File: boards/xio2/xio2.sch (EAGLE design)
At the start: 337 parts, among them J1 12401598E4#2A, Q1 BSS138, Q2 BSS138, Q3 BC817-16LT3G, Q4 BC817-16LT3G, X1 MINI-USB-UX60-MB-5ST, Y2 FA-238 25.0000MB-K3

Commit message: Latest schematic and routed board
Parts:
- renumbered CART_SLOT to HOST_IO, U$1 to XIO, X1 to USB
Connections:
- net N$1 renamed XIO_CLK_OUT
- net N$2 renamed XIO_CLK_IN

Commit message: Update some BOM-related things
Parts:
- C105, C93, C95: device rcl:C-EUC0402 -> rcl:C-EUC0402K
- C177: device rcl:C-EUC0201 -> rcl:C-EUC0402
- CARTRIDGE: value A8_CART -> 5650118-1

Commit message: Some small notes on layout
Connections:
- net N$72 renamed XSPI5_MISO_R
- net N$73 renamed XSPI5_MOSI_R
- net N$74 renamed XSPI5_SCK_R
- net N$75 renamed XSPI6_MISO_R
- net N$79 renamed XSPI6_SCK_R
- net N$98 renamed XSPI6_MOSI_R
- net XPSI5_MOSI renamed XSPI5_MOSI
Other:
- moved on the sheet: R91, R92, R93

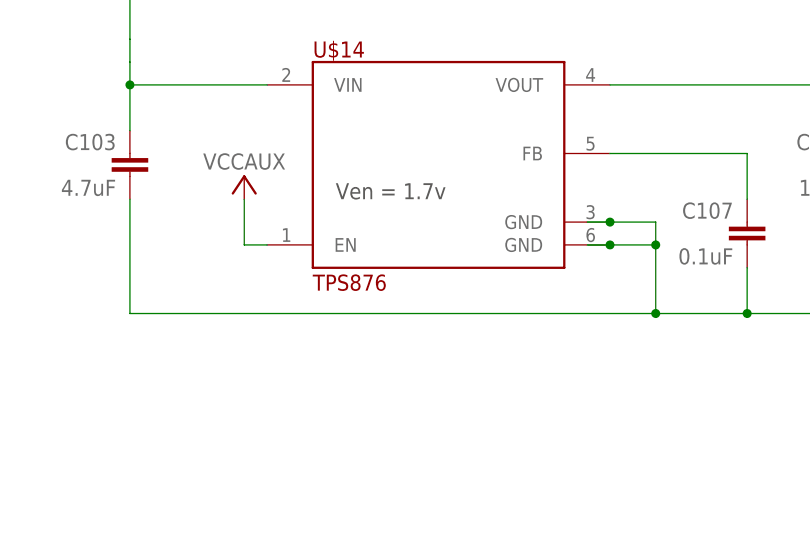
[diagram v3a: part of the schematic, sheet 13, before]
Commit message: Update the TI vreg
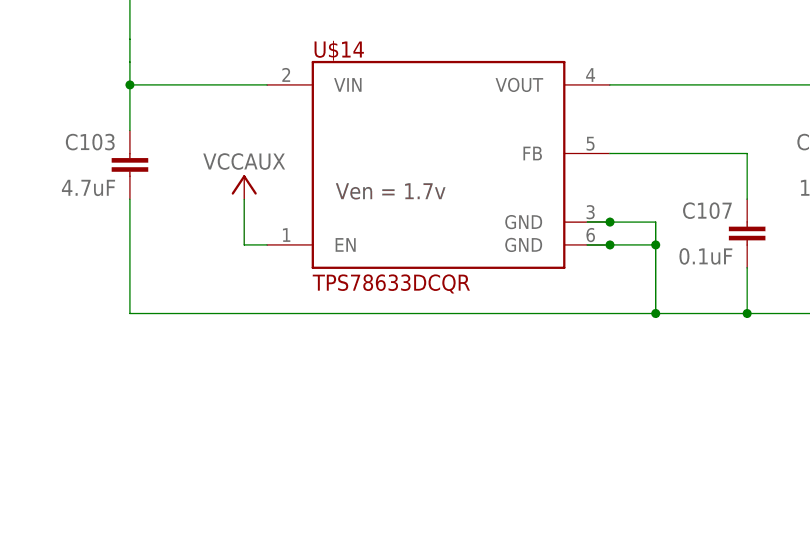
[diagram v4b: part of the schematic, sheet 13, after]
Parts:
- U$14: value TPS876 -> TPS78633DCQR
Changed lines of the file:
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@@
 <part name="LED3" library="led" library_urn="urn:adsk.eagle:library:259" deviceset="LED" device="CHIPLED_0603" package3d_urn="urn:adsk.eagle:package:15822/2" value="LTST-S270GKT"/>
 <part name="SUPPLY90" library="supply2" deviceset="GND" device=""/>
-<part name="U$14" library="sjg-power" deviceset="TPS876" device="" package3d_urn="urn:adsk.eagle:package:4768344/1"/>
+<part name="U$14" library="sjg-power" deviceset="TPS876" device="" package3d_urn="urn:adsk.eagle:package:4768344/1" value="TPS78633DCQR"/>
 <part name="C107" library="rcl" library_urn="urn:adsk.eagle:library:334" deviceset="C-EU" device="C0201" package3d_urn="urn:adsk.eagle:package:23690/2" value="0.1uF"/>
 <part name="C103" library="rcl" library_urn="urn:adsk.eagle:library:334" deviceset="C-EU" device="C0402" package3d_urn="urn:adsk.eagle:package:23626/1" value="4.7uF"/>

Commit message: Design review first changes
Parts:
- renumbered U$14 to FPGA_VCCO
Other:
- note added: "TMDS_33 signalling requires 50R pull-ups to 3.3v on all inputs. Labels {RX*,TX*} are from perspective of the host board, so need to add pull-ups to TX* lines on this board. Will dissipate 66mA, so need to be 0603"
- note removed: "TMDS_33 signalling requires 50R pull-ups to 3.3v on all inputs. Labels {RX*,TX*} are from perspective of the host board, so need to add pull-ups to TX* lines on this board."
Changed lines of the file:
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@@
 <part name="LED3" library="led" library_urn="urn:adsk.eagle:library:259" deviceset="LED" device="CHIPLED_0603" package3d_urn="urn:adsk.eagle:package:15822/2" value="LTST-S270GKT"/>
 <part name="SUPPLY90" library="supply2" deviceset="GND" device=""/>
-<part name="U$14" library="sjg-power" deviceset="TPS876" device="" package3d_urn="urn:adsk.eagle:package:4768344/1" value="TPS78633DCQR"/>
+<part name="FPGA_VCCO" library="sjg-power" deviceset="TPS876" device="" package3d_urn="urn:adsk.eagle:package:4768344/1" value="TPS78633DCQR"/>
 <part name="C107" library="rcl" library_urn="urn:adsk.eagle:library:334" deviceset="C-EU" device="C0201" package3d_urn="urn:adsk.eagle:package:23690/2" value="0.1uF"/>
 <part name="C103" library="rcl" library_urn="urn:adsk.eagle:library:334" deviceset="C-EU" device="C0402" package3d_urn="urn:adsk.eagle:package:23626/1" value="4.7uF"/>
@@
 <pinref part="+3V23" gate="G$1" pin="+3V3"/>
 <wire x1="96.52" y1="93.98" x2="96.52" y2="99.06" width="0.1524" layer="91"/>
+<label x="93.98" y="104.14" size="1.778" layer="95"/>
 </segment>
 </net>
@@
 <wire x1="-124.46" y1="76.2" x2="-124.46" y2="78.74" width="0.1524" layer="91"/>
 <junction x="-124.46" y="78.74"/>
+<label x="-127" y="96.52" size="1.778" layer="95"/>
 </segment>
 <segment>
@@
 <wire x1="-127" y1="-35.56" x2="-127" y2="-33.02" width="0.1524" layer="91"/>
 <junction x="-127" y="-33.02"/>
+<label x="-129.54" y="-20.32" size="1.778" layer="95"/>
 </segment>
 <segment>
@@
 <wire x1="-127" y1="22.86" x2="-127" y2="25.4" width="0.1524" layer="91"/>
 <junction x="-127" y="25.4"/>
+<label x="-129.54" y="40.64" size="1.778" layer="95"/>
 </segment>
 </net>
@@
 <instance part="U$7" gate="G$1" x="73.66" y="63.5"/>
 <instance part="U$8" gate="G$1" x="73.66" y="104.14"/>
-<instance part="U$14" gate="G$1" x="-124.46" y="-86.36"/>
+<instance part="FPGA_VCCO" gate="G$1" x="-124.46" y="-86.36"/>
 <instance part="C107" gate="G$1" x="-88.9" y="-93.98" rot="MR0"/>
 <instance part="C103" gate="G$1" x="-157.48" y="-86.36" rot="MR0"/>
@@
 <wire x1="-99.06" y1="-93.98" x2="-99.06" y2="-96.52" width="0.1524" layer="91"/>
 <junction x="-99.06" y="-96.52"/>
-<pinref part="U$14" gate="G$1" pin="GND@TAB"/>
+<pinref part="FPGA_VCCO" gate="G$1" pin="GND@TAB"/>
 <junction x="-104.14" y="-96.52"/>
-<pinref part="U$14" gate="G$1" pin="GND@3"/>
+<pinref part="FPGA_VCCO" gate="G$1" pin="GND@3"/>
 <junction x="-104.14" y="-93.98"/>
 <pinref part="C107" gate="G$1" pin="2"/>
@@
 <wire x1="-144.78" y1="-96.52" x2="-144.78" y2="-91.44" width="0.1524" layer="91"/>
 <pinref part="U$6" gate="G$1" pin="VCCAUX"/>
-<pinref part="U$14" gate="G$1" pin="EN@1"/>
+<pinref part="FPGA_VCCO" gate="G$1" pin="EN@1"/>
 </segment>
 <segment>
@@
 <wire x1="-157.48" y1="-83.82" x2="-157.48" y2="-78.74" width="0.1524" layer="91"/>
 <pinref part="C103" gate="G$1" pin="1"/>
-<pinref part="U$14" gate="G$1" pin="VIN@2"/>
+<pinref part="FPGA_VCCO" gate="G$1" pin="VIN@2"/>
 <wire x1="-157.48" y1="-78.74" x2="-157.48" y2="-76.2" width="0.1524" layer="91"/>
 <wire x1="-142.24" y1="-78.74" x2="-157.48" y2="-78.74" width="0.1524" layer="91"/>
@@
 <segment>
 <pinref part="C107" gate="G$1" pin="1"/>
-<pinref part="U$14" gate="G$1" pin="FB@5"/>
+<pinref part="FPGA_VCCO" gate="G$1" pin="FB@5"/>
 <wire x1="-88.9" y1="-91.44" x2="-88.9" y2="-86.36" width="0.1524" layer="91"/>
 <wire x1="-88.9" y1="-86.36" x2="-104.14" y2="-86.36" width="0.1524" layer="91"/>
@@
 <pinref part="C105" gate="G$1" pin="1"/>
 <wire x1="-76.2" y1="-83.82" x2="-76.2" y2="-78.74" width="0.1524" layer="91"/>
-<pinref part="U$14" gate="G$1" pin="VOUT@4"/>
+<pinref part="FPGA_VCCO" gate="G$1" pin="VOUT@4"/>
 <wire x1="-76.2" y1="-78.74" x2="-76.2" y2="-76.2" width="0.1524" layer="91"/>
 <wire x1="-104.14" y1="-78.74" x2="-76.2" y2="-78.74" width="0.1524" layer="91"/>
@@
 <text x="-185.42" y="119.38" size="1.778" layer="94">USB3 connections</text>
 <text x="143.51" y="-103.886" size="2.1844" layer="94">FPGA Bank 14</text>
-<text x="-160.02" y="-101.6" size="1.778" layer="97">TMDS_33 signalling requires 50R
+<text x="-160.02" y="-106.68" size="1.778" layer="97">TMDS_33 signalling requires 50R
 pull-ups to 3.3v on all inputs.
 Labels {RX*,TX*} are from perspective
 of the host board, so need to add
-pull-ups to TX* lines on this board.</text>
+pull-ups to TX* lines on this board.
+Will dissipate 66mA, so need to be 0603</text>
 <text x="-160.02" y="-83.82" size="1.778" layer="94">Pull-up specification</text>
 <wire x1="-162.56" y1="-78.74" x2="-111.76" y2="-78.74" width="0.1524" layer="97"/>
-<wire x1="-111.76" y1="-78.74" x2="-111.76" y2="-104.14" width="0.1524" layer="97"/>
-<wire x1="-111.76" y1="-104.14" x2="-162.56" y2="-104.14" width="0.1524" layer="97"/>
-<wire x1="-162.56" y1="-104.14" x2="-162.56" y2="-78.74" width="0.1524" layer="97"/>
+<wire x1="-111.76" y1="-78.74" x2="-111.76" y2="-109.22" width="0.1524" layer="97"/>
+<wire x1="-111.76" y1="-109.22" x2="-162.56" y2="-109.22" width="0.1524" layer="97"/>
+<wire x1="-162.56" y1="-109.22" x2="-162.56" y2="-78.74" width="0.1524" layer="97"/>
 </plain>
 <instances>

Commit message: Simple changes from design reviews completed.
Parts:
- added BOOT_MODE: 209-3MS, special:SW_DIP-3
- added R119: 100K, rcl:R-EU_R0201
- added R120, R121: 10K, rcl:R-EU_R0201
- added R122, R123, R124, R128: 1K, rcl:R-EU_R0201
- added R125, R126, R127: 47K, rcl:R-EU_R0201
- C173: value 0.1uF -> 1uF
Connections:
- net SPI_IRQ renamed !SPI_IRQ!
- new net BOOT_M0: BOOT_MODE.1, R127.1, S7-25-CFG.M0_0@M7
- new net BOOT_M1: BOOT_MODE.2, R126.1, S7-25-CFG.M1_0@M8
- new net BOOT_M2: BOOT_MODE.3, R125.1, S7-25-CFG.M2_0@M9
- new net N$11: ARCH_ID.5, ARCH_ID.6, ARCH_ID.7, ARCH_ID.8, R122.2
- new net N$2: R121.2, SDRAM.CKE@67
- new net N$48: MEM_ID.3, MEM_ID.4, R123.2
- new net N$49: PID.4, PID.5, PID.6, R124.2
- new net N$50: BOOT_MODE.4, BOOT_MODE.5, BOOT_MODE.6, R128.2
- new net N$7: R120.1, SDRAM.!CS!@20
- net +3V3: now also R121.1, R122.1, R123.1, R124.1, R128.1; no longer ARCH_ID.5, ARCH_ID.6, ARCH_ID.7, ARCH_ID.8, LVL_RD4.DIR@5, LVL_RD5.DIR@5, MEM_ID.3, MEM_ID.4, MUX-HI.VCC@16, MUX-LO.VCC@16, PID.4, PID.5, PID.6, S7-25-CFG.M0_0@M7, SDRAM.CKE@67
- net +5V: now also LVL_RD4.DIR@5, LVL_RD5.DIR@5, R119.1
- net GND: now also R120.2, R125.2, R126.2, R127.2; no longer S7-25-CFG.M1_0@M8, S7-25-CFG.M2_0@M9, SDRAM.!CS!@20
- net N$65: now also R119.2
- net VCCO: now also MUX-HI.VCC@16, MUX-LO.VCC@16
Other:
- note added: "5v-in is ok to NC"
- note added: "Boot mode"
- note added: "JTAG mode: Set M[2:0] to 101 Master SPI : Set M[2:0] to 001"
- note removed: "Master QSPI config mode"
- moved on the sheet: C173, PSW, S7-25-ADC, XIO-USB

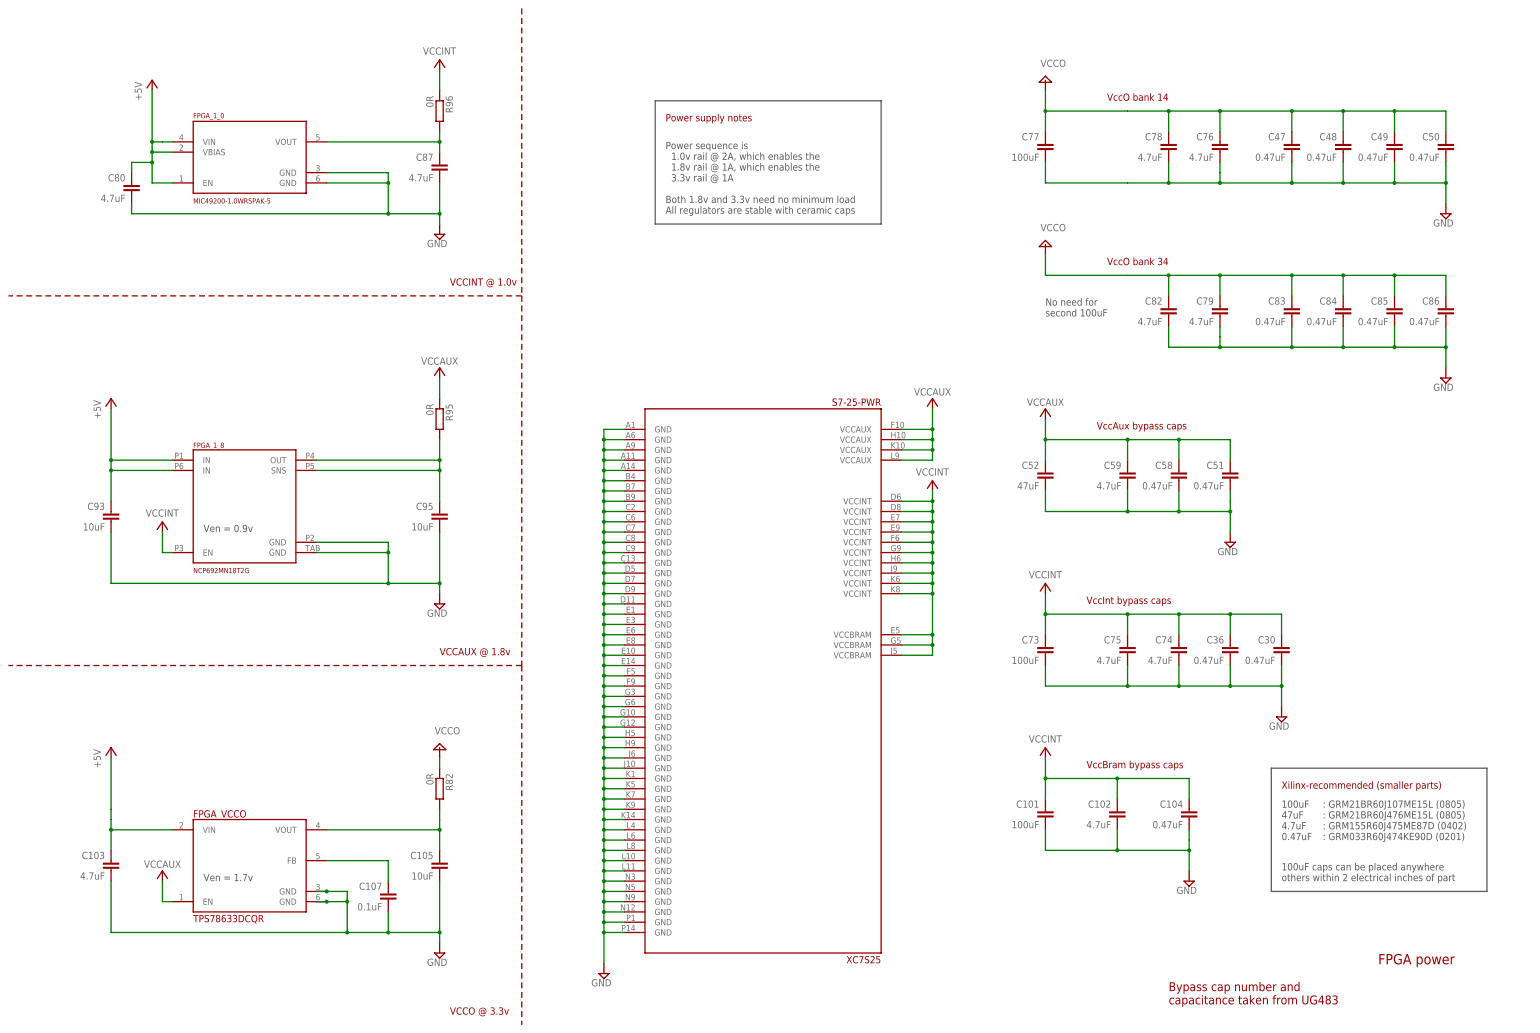
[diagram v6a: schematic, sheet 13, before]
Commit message: Incorporate the changes from the design-review, including switching regulator for 1.0v
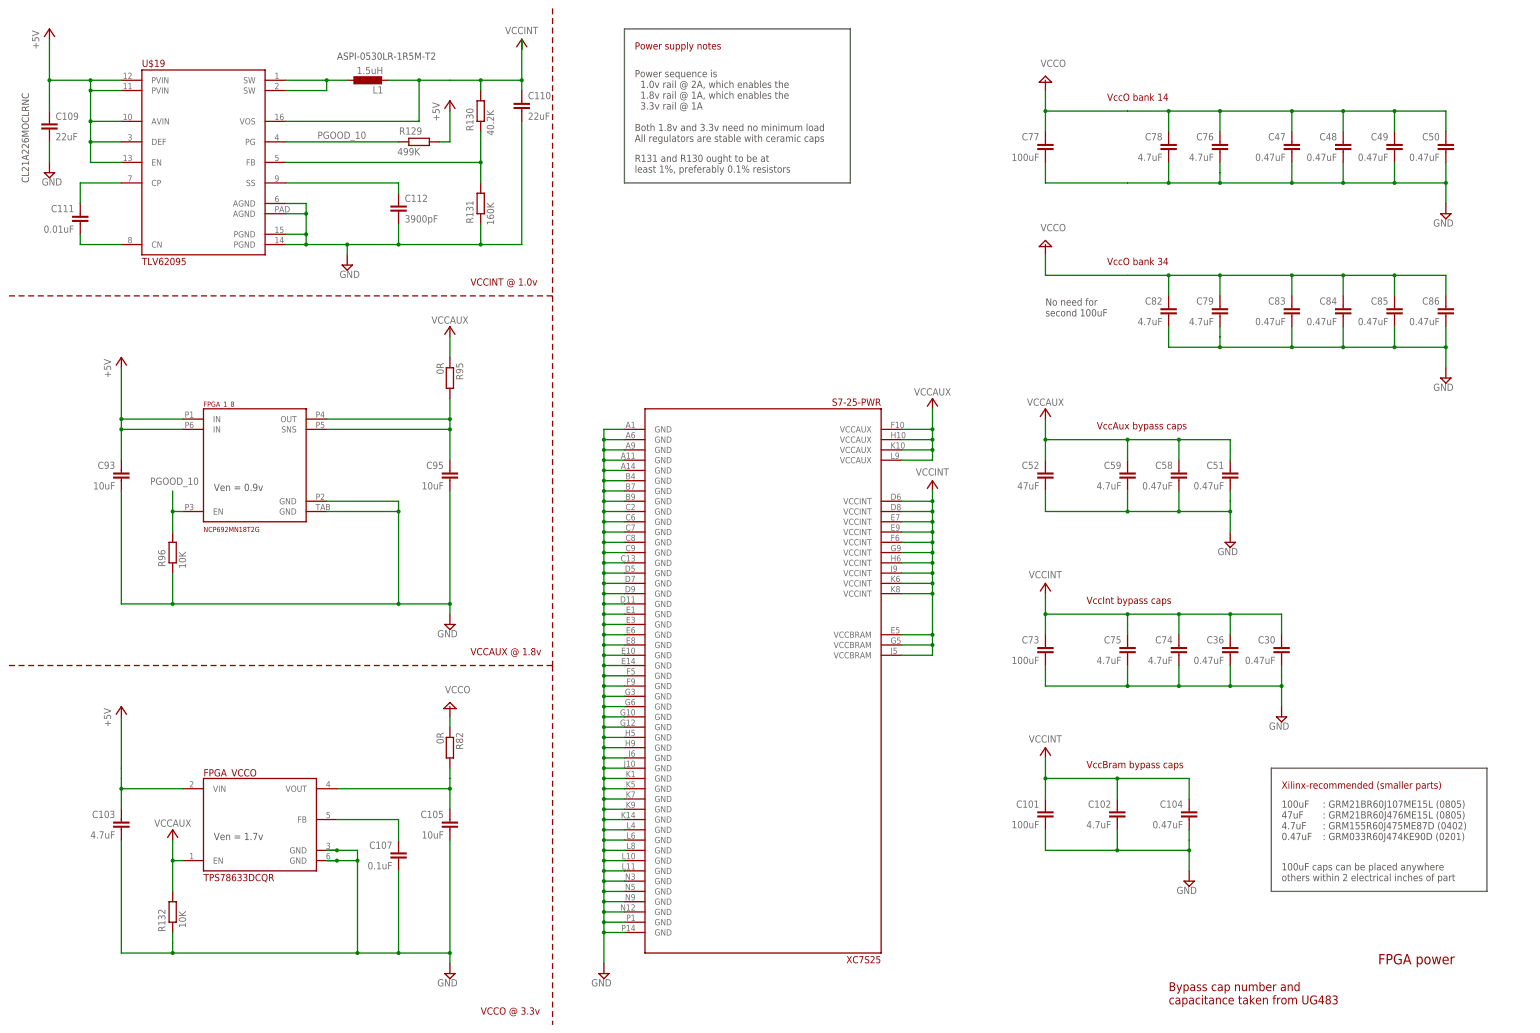
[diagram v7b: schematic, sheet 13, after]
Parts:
- removed C80, C87: 4.7uF, rcl:C-EUC0402
- removed FPGA_1_0: MIC49200-1.0WRSPAK-5, sjg-power:MIC49200-1.0WRSPAK-5
- added C109, C110: 22uF, rcl:C-EUC0603
- added C111: 0.01uF, rcl:C-EUC0402
- added C112: 3900pF, rcl:C-EUC0402
- added L1: 1.5uH, rcl:L-EUL5650M
- added R129: 499K, rcl:R-EU_R0402
- added R130: 40.2K, rcl:R-EU_R0402
- added R131: 160K, rcl:R-EU_R0402
- added R132: 10K, rcl:R-EU_R0402
- added U$19: TLV62095, sjg-power:TLV62095
- R96: value 0R -> 10K
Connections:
- removed net N$83: C87.1, FPGA_1_0.VOUT@5, R96.2
- new net N$64: C111.1, U$19.CP@7
- new net N$72: C111.2, U$19.CN@8
- new net N$73: L1.1, U$19.SW@1, U$19.SW@2
- new net N$79: R130.2, R131.1, U$19.FB@5
- new net N$98: C112.1, U$19.SS@9
- new net PGOOD_10: FPGA_1_8.EN@3, R129.2, R96.1, U$19.PG@4
- net +5V: now also C109.1, R129.1, U$19.AVIN@10, U$19.DEF@3, U$19.EN@13, U$19.PVIN@11, U$19.PVIN@12; no longer C80.1, FPGA_1_0.EN@1, FPGA_1_0.VBIAS@2, FPGA_1_0.VIN@4
- net GND: now also C109.2, C110.2, C112.2, R131.2, R132.2, R96.2, U$19.AGND@6, U$19.AGND@PAD, U$19.PGND@14, U$19.PGND@15; no longer C80.2, C87.2, FPGA_1_0.GND@3, FPGA_1_0.GND@TAB
- net VCCAUX: now also R132.1
- net VCCINT: now also C110.1, L1.2, R130.1, U$19.VOS@16; no longer FPGA_1_8.EN@3, R96.1
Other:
- note added: "ASPI-0530LR-1R5M-T2"
- note added: "CL21A226MOCLRNC"
- note added: "R131 and R130 ought to be at least 1%, preferably 0.1% resistors"
- moved on the sheet: C103, C105, C107, C93, C95, FPGA_1_8, FPGA_VCCO, PSW, R82, R95, R96, XIO-USB
